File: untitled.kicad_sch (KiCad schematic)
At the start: 10 parts, among them U1 LM2576HVT-5, U2 LM2576HVT-12

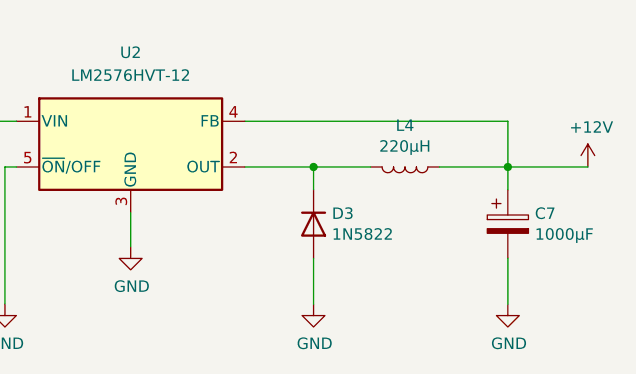
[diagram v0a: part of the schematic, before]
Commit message: place components on pcb
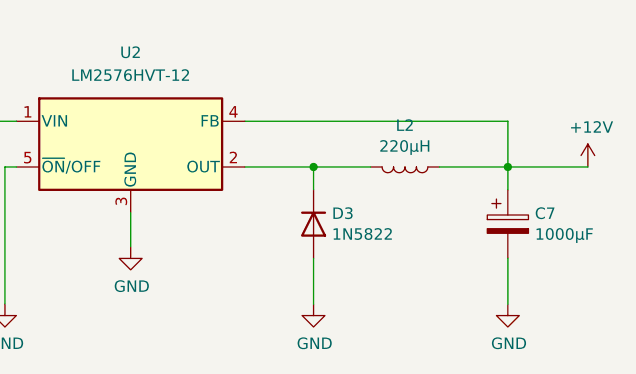
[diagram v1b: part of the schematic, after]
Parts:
- L1: footprint Inductor_SMD:L_TDK_SLF10145 -> CNC_interface:L_Radial_24.4mm_P23.50mm_Murata_1400series
- L2: renamed from L4; footprint Inductor_SMD:L_TDK_SLF10145 -> CNC_interface:L_Radial_24.4mm_P23.50mm_Murata_1400series
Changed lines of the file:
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@@
   (symbol (lib_id "Device:L") (at 217.17 49.53 270) (unit 1)
     (in_bom yes) (on_board yes)
-    (property "Reference" "L4" (id 0) (at 217.17 44.9326 90))
+    (property "Reference" "L2" (id 0) (at 217.17 44.9326 90))
     (property "Value" "220µH" (id 1) (at 217.17 47.244 90))
-    (property "Footprint" "Inductor_SMD:L_TDK_SLF10145" (id 2) (at 217.17 49.53 0)
+    (property "Footprint" "CNC_interface:L_Radial_24.4mm_P23.50mm_Murata_1400series" (id 2) (at 217.17 49.53 0)
       (effects (font (size 1.27 1.27)) hide)
     )
@@
     (property "Reference" "L1" (id 0) (at 109.22 42.3926 90))
     (property "Value" "150µF" (id 1) (at 109.22 44.704 90))
-    (property "Footprint" "Inductor_SMD:L_TDK_SLF10145" (id 2) (at 109.22 46.99 0)
+    (property "Footprint" "CNC_interface:L_Radial_24.4mm_P23.50mm_Murata_1400series" (id 2) (at 109.22 46.99 0)
       (effects (font (size 1.27 1.27)) hide)
     )

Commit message: connect step motors to 12V
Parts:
- C1, C6: footprint Capacitor_THT:CP_Radial_D12.5mm_P5.00mm -> Capacitor_THT:CP_Radial_D6.3mm_P2.50mm
- C2, C7: footprint Capacitor_THT:CP_Radial_D8.0mm_P3.50mm -> Capacitor_THT:CP_Radial_D12.5mm_P5.00mm
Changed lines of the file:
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@@
       (effects (font (size 1.27 1.27)) (justify left))
     )
-    (property "Footprint" "Capacitor_THT:CP_Radial_D12.5mm_P5.00mm" (id 2) (at 56.8452 57.15 0)
+    (property "Footprint" "Capacitor_THT:CP_Radial_D6.3mm_P2.50mm" (id 2) (at 56.8452 57.15 0)
       (effects (font (size 1.27 1.27)) hide)
     )
@@
       (effects (font (size 1.27 1.27)) (justify left))
     )
-    (property "Footprint" "Capacitor_THT:CP_Radial_D12.5mm_P5.00mm" (id 2) (at 164.7952 59.69 0)
+    (property "Footprint" "Capacitor_THT:CP_Radial_D6.3mm_P2.50mm" (id 2) (at 164.7952 59.69 0)
       (effects (font (size 1.27 1.27)) hide)
     )
@@
       (effects (font (size 1.27 1.27)) (justify left))
     )
-    (property "Footprint" "Capacitor_THT:CP_Radial_D8.0mm_P3.50mm" (id 2) (at 121.6152 57.15 0)
+    (property "Footprint" "Capacitor_THT:CP_Radial_D12.5mm_P5.00mm" (id 2) (at 121.6152 57.15 0)
       (effects (font (size 1.27 1.27)) hide)
     )
@@
       (effects (font (size 1.27 1.27)) (justify left))
     )
-    (property "Footprint" "Capacitor_THT:CP_Radial_D8.0mm_P3.50mm" (id 2) (at 229.5652 59.69 0)
-      (effects (font (size 1.27 1.27)) hide)
-    )
+    (property "Footprint" "Capacitor_THT:CP_Radial_D12.5mm_P5.00mm" (id 2) (at 229.5652 59.69 0)
+      (effects (font (size 1.27 1.27)) hide)
+    )

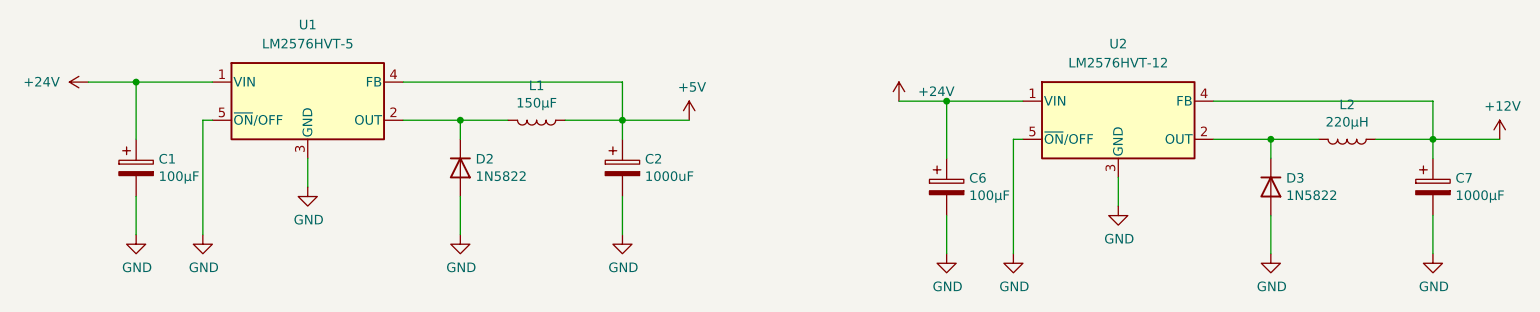
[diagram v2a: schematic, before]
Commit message: place components
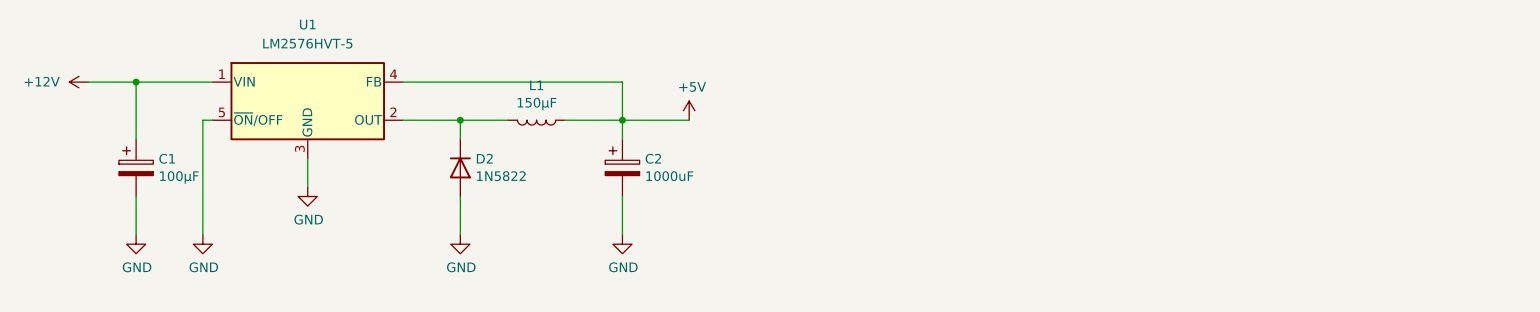
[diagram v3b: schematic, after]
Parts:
- removed C6: 100µF, Capacitor_THT:CP_Radial_D6.3mm_P2.50mm, symbol Device:CP
- removed C7: 1000µF, Capacitor_THT:CP_Radial_D12.5mm_P5.00mm, symbol Device:CP
- removed D3: 1N5822, Diode_THT:D_DO-201AD_P15.24mm_Horizontal, symbol Device:D
- removed L2: 220µH, CNC_interface:L_Radial_24.4mm_P23.50mm_Murata_1400series, symbol Device:L
- removed U2: LM2576HVT-12, Package_TO_SOT_THT:TO-220-5_Vertical, symbol Regulator_Switching:LM2576HVT-12
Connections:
- net +24V is gone; now on net +12V: C1.1, U1.1 (VIN)
